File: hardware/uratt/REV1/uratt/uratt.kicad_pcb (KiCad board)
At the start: 4 copper layers, 62 x 71.4 mm, 143 parts, among them J1 USB_B_Micro, J2 Micro_SD_Card, J3 Conn_01x10, J4 Conn_01x04, J5 Conn_01x04, J6 Conn_01x02, J7 Conn_01x02, J8 Conn_01x02, Q1 MMBT3904, Q2 MMBT3904, Q3 2N7002, Q4 DMP31D0U, SW1 SW_Push, SW2 SW_Push, SW3 SW_SPDT, U1 SN65220DBVR, U2 CP2102N-A02-GQFN24, U3 ESP32-WROOM-32E, U4 MCP73832T-2ACI/OT, U5 TPS2115APWR, U6 AP2112K-3.3TRG1, U7 AP2112K-3.3TRG1, U8 TPS61032PWP, U9 MP6513GJ-Z

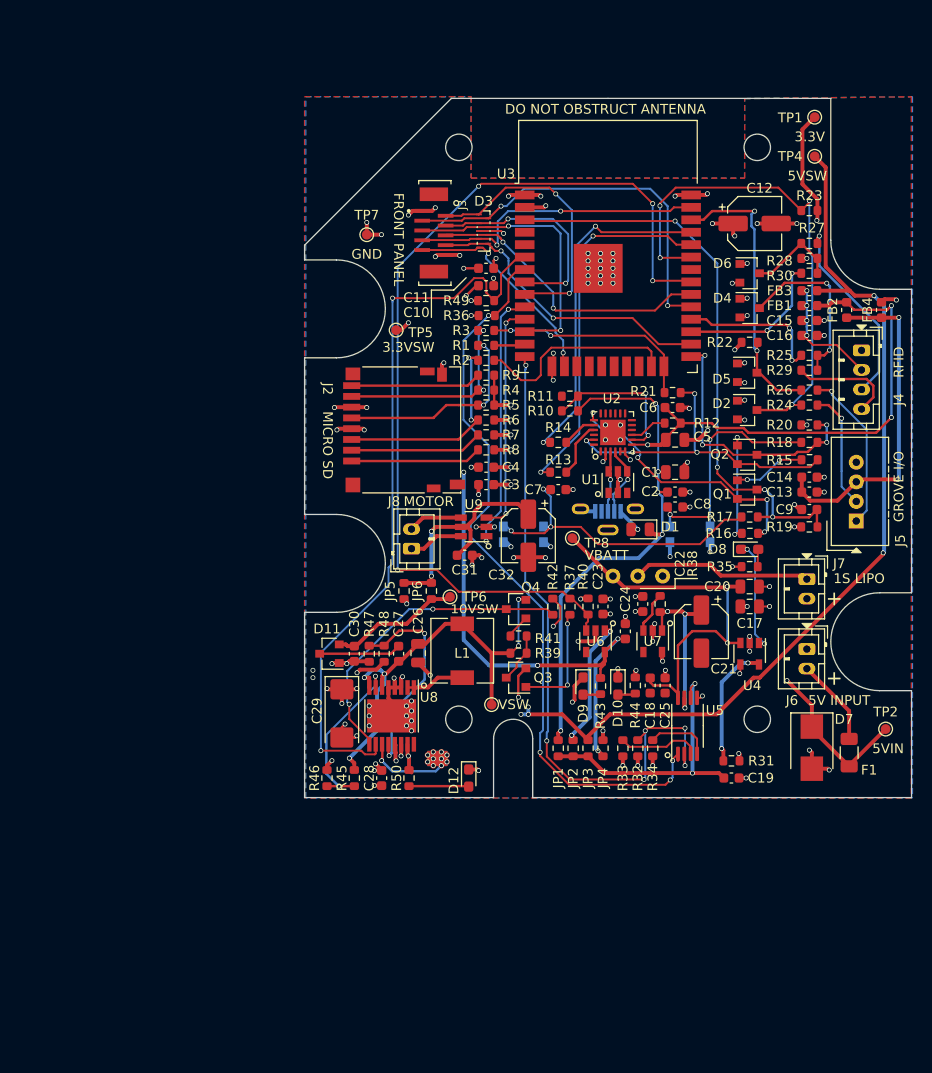
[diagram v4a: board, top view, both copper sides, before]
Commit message: complete relayout of 5V boost switcher, add plated mount holes w/FB GND ties, passes DRC
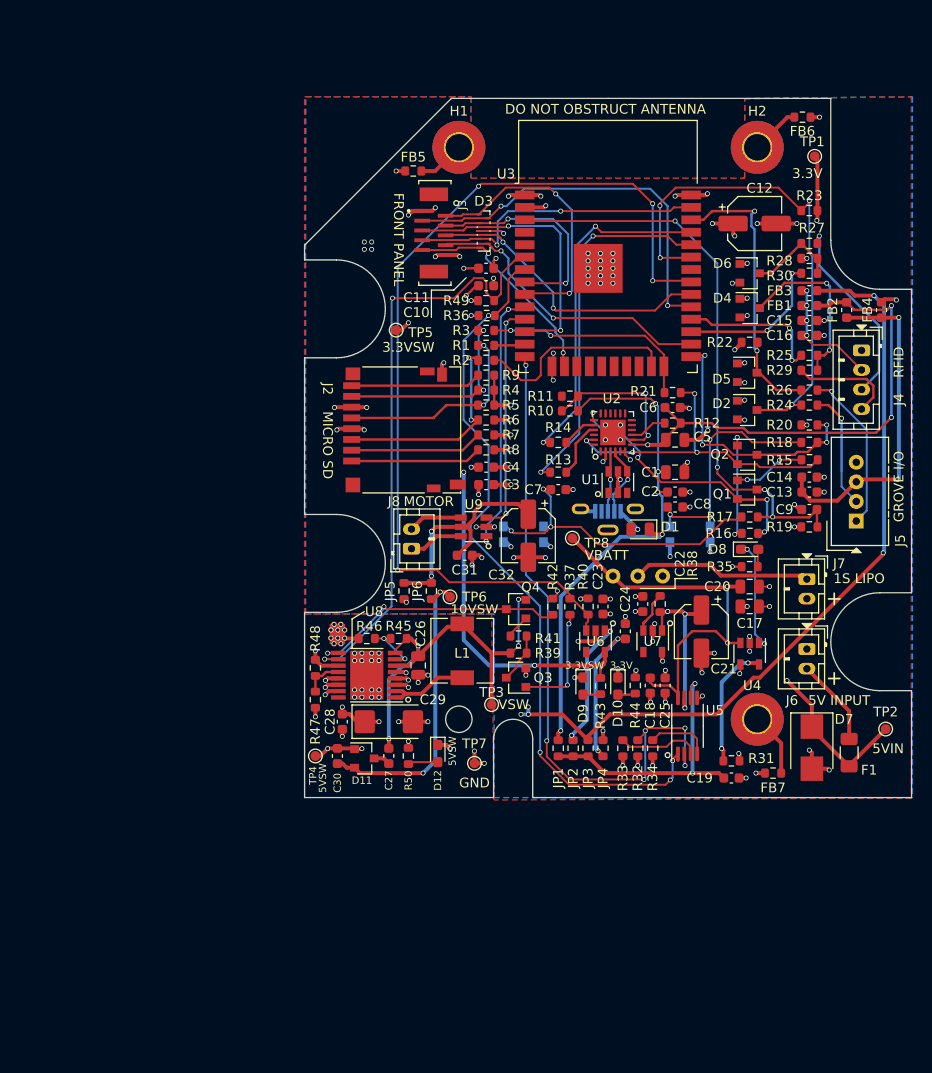
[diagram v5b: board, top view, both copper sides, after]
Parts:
- added FB5: OPTION, Resistor_SMD:R_0603_1608Metric, F.Cu at (36.2, 30.0)
- added FB6: OPTION, Resistor_SMD:R_0603_1608Metric, F.Cu at (76.0, 24.5)
- added FB7: OPTION, Resistor_SMD:R_0603_1608Metric, F.Cu at (73.0, 91.5)
- H1, H2, H4: value MountingHole -> MountingHole_Pad; footprint MountingHole:MountingHole_2.7mm_M2.5 -> MountingHole:MountingHole_2.7mm_M2.5_Pad_TopBottom
- moved TP4 79.7 mm to (26.2, 89.8), turned to 90 degrees
- moved TP7 55.1 mm to (42.5, 90.5)
- moved GT1 17.0 mm to (29.2, 76.9), turned to 270 degrees
- moved R45 15.0 mm to (34.8, 77.8), turned to 0 degrees
- moved R46 14.8 mm to (31.5, 77.8), turned to 0 degrees
- moved D11 11.3 mm to (31.2, 90.0), turned to 0 degrees
- moved C30 10.6 mm to (28.5, 89.8), turned to 90 degrees
- moved C27 10.5 mm to (33.8, 89.8), turned to 90 degrees
- moved R47 7.23 mm to (26.2, 84.0)
- moved R48 7.17 mm to (26.2, 80.8), turned to 270 degrees
- moved C28 7.02 mm to (29.0, 86.2)
- moved U8 4.87 mm to (31.5, 81.5), turned to 90 degrees
- moved C29 4.87 mm to (33.8, 86.2), turned to 0 degrees
- moved D12 4.03 mm to (38.8, 89.5)
- moved TP1 4.00 mm to (77.2, 28.5)
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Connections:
- H1 pad 1: (no net) -> Net-(FB5-Pad2)
- H2 pad 1: (no net) -> Net-(FB6-Pad2)
- H4 pad 1: (no net) -> Net-(FB7-Pad2)
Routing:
- net Net-(R47-Pad1): track 21.6 -> 4.12 mm, vias 2 -> 0
- net +10VSW: track 13.5 -> 30.8 mm, vias 0 -> 2
- net +5VSW: track 112.6 -> 96.2 mm, vias 16 -> 15
- net LOW_BAT: track 75.0 -> 61.0 mm
- net Net-(R45-Pad1): track 17.8 -> 5.63 mm
- net GNDPWR: track 13.3 -> 21.9 mm, vias 22 -> 29
- net Net-(C27-Pad1): track 8.39 -> 1.72 mm
- net Net-(FB7-Pad2): track 0.00 -> 6.51 mm
- net Net-(Q4-Pad3): track 32.3 -> 26.8 mm
- net Net-(FB6-Pad2): track 0.00 -> 5.06 mm
- net +3V3: track 32.7 -> 27.7 mm
- net Net-(FB5-Pad2): track 0.00 -> 4.83 mm
- net GND: track 105.4 -> 102.0 mm, vias 100 -> 108
- net Net-(D12-Pad2): track 6.12 -> 3.08 mm
- net Net-(L1-Pad2): track 6.01 -> 8.84 mm
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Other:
- board text added: "REV1 / 2021-JAN-13"
- board text removed: "REV1 / 20201-XXX-XX"

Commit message: add breakaway rails & fiducials for assembly
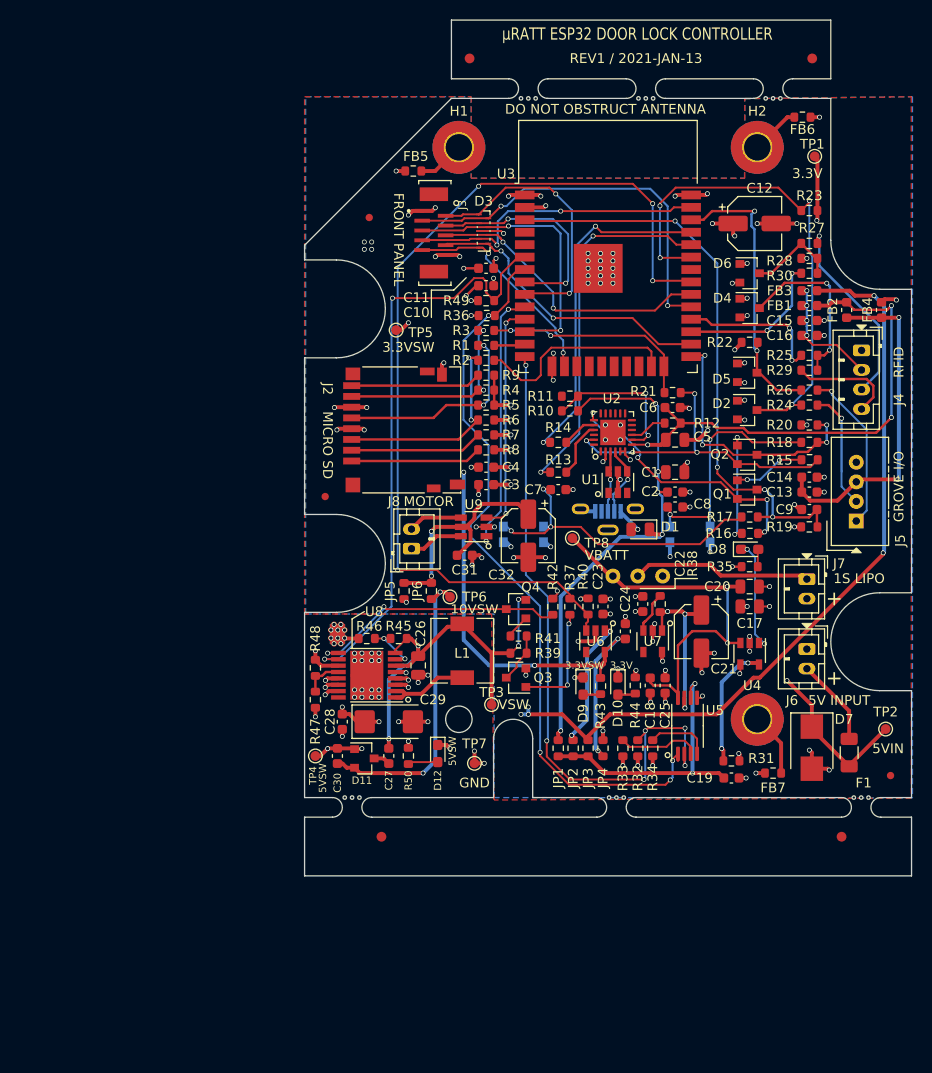
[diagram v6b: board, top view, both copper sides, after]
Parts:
- added BK1: BREAKAWAY, uratt:RATT_BITE, F.Cu at (50.0, 22.6)
- added BK2: BREAKAWAY, uratt:RATT_BITE, F.Cu at (75.0, 22.6)
- added BK3: BREAKAWAY, uratt:RATT_BITE, F.Cu at (62.0, 22.6)
- added BK4: BREAKAWAY, uratt:RATT_BITE, F.Cu at (28.0, 94.0)
- added BK5: BREAKAWAY, uratt:RATT_BITE, F.Cu at (55.0, 94.0)
- added BK6: BREAKAWAY, uratt:RATT_BITE, F.Cu at (80.0, 94.0)
- added FID1: Fiducial, Fiducial:Fiducial_1mm_Mask3mm, F.Cu at (42.0, 18.5)
- added FID2: Fiducial, Fiducial:Fiducial_1mm_Mask3mm, F.Cu at (77.0, 18.5)
- added FID3: Fiducial, Fiducial:Fiducial_1mm_Mask3mm, F.Cu at (33.0, 98.0)
- added FID4: Fiducial, Fiducial:Fiducial_1mm_Mask3mm, F.Cu at (80.0, 98.0)
- added FID5: Fiducial, Fiducial:Fiducial_0.75mm_Mask1.5mm, F.Cu at (31.8, 34.8)
- added FID6: Fiducial, Fiducial:Fiducial_0.75mm_Mask1.5mm, F.Cu at (85.0, 91.8)
- added FID7: Fiducial, Fiducial:Fiducial_0.75mm_Mask1.5mm, F.Cu at (27.2, 63.2)
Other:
- board size 62 x 71.4 mm -> 62 x 87.4 mm

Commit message: uratt REV1 change inductor, cleanups, add 3.3V motor option, silk work, 12 pin FFC
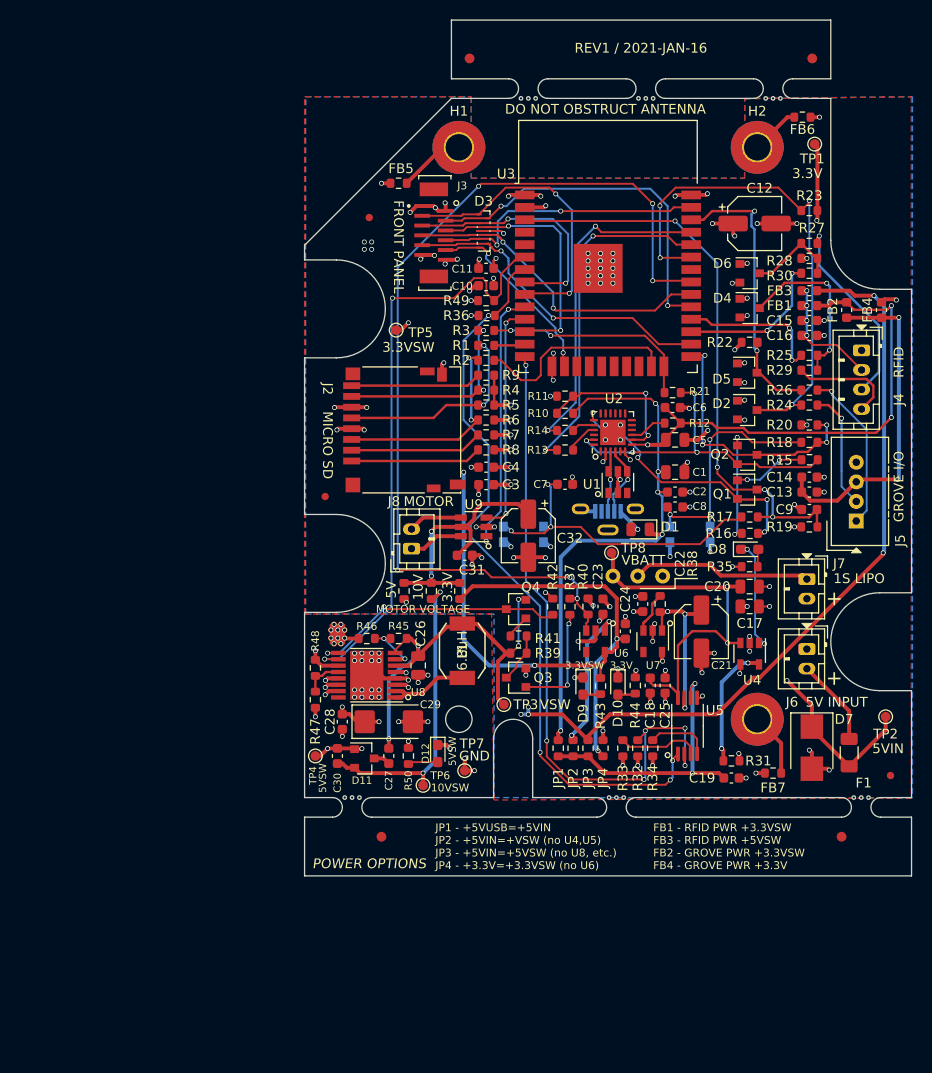
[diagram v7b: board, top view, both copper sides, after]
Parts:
- added JP7: 0 (OPTION), Resistor_SMD:R_0603_1608Metric, F.Cu at (41.0, 72.9)
- J3: footprint uratt:TE_1-1734742-0 -> uratt:TE_1-1734742-2
- L1: footprint Inductor_SMD:L_6.3x6.3_H3 -> uratt:SRR6603-6R8ML
- moved TP6 19.4 mm to (37.2, 92.8)
- moved TP8 4.27 mm to (56.5, 69.0)
- moved R13 2.37 mm to (51.8, 58.5)
- moved FB5 1.95 mm to (34.8, 31.2)
- moved R14 1.40 mm to (51.8, 56.5)
- moved TP1 1.25 mm to (77.2, 27.2)
- moved TP2 1.25 mm to (84.5, 85.8)
- moved TP3 1.25 mm to (45.5, 84.5)
- moved TP7 1.25 mm to (41.5, 91.2)
- moved C7 0.88 mm to (51.8, 62.0)
- moved R10 0.56 mm to (51.8, 54.8)
- moved R11 0.50 mm to (51.8, 53.0)
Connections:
- J3 pad 10: GND -> FP_TOUCH_BTN
- J3 pad 2: LCD_BL -> +3.3VSW
- J3 pad 3: LCD_CS -> LCD_BL
- J3 pad 4: LCD_RESET -> LCD_CS
- J3 pad 5: LCD_DC -> LCD_RESET
- J3 pad 6: LCD_CLK -> LCD_DC
- J3 pad 7: LCD_MOSI -> LCD_CLK
- J3 pad 8: BEEPER -> LCD_MOSI
- J3 pad 9: FP_TOUCH_BTN -> BEEPER
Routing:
- net +3.3VSW: track 125.6 -> 148.2 mm, vias 19 -> 20
- net +VBATT: track 42.1 -> 39.1 mm
- net +5VUSB: track 53.4 -> 56.4 mm
- net Net-(C31-Pad1): track 24.3 -> 27.2 mm
- net Net-(R13-Pad2): track 5.75 -> 3.26 mm
- net LCD_CS: track 39.8 -> 37.4 mm
- net LCD_DC: track 28.3 -> 25.9 mm
- net LCD_RESET: track 22.8 -> 25.2 mm
- net LCD_MOSI: track 30.8 -> 28.4 mm
- net LCD_BL: track 28.3 -> 30.7 mm
- net FP_TOUCH_BTN: track 22.1 -> 19.7 mm
- net BEEPER: track 30.5 -> 32.9 mm
- net LCD_CLK: track 30.0 -> 32.4 mm
- net +VSW: track 75.3 -> 77.7 mm
- net RXD0: track 37.7 -> 35.4 mm
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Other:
- board text added: "10V"
- board text added: "5V"
- board text added: "BOARD NUM."
- board text added: "FB1 - RFID PWR +3.3VSW FB3 - RFID PWR +5VSW FB2 - GROVE PWR +3.3VSW FB4 - GROVE PWR +3.3V"
- board text added: "JP1 - +5VUSB=+5VIN JP2 - +5VIN=+VSW (no U4,U5) JP3 - +5VIN=+5VSW (no U8, etc.) JP4 - +3.3V=+3.3VSW (no U6)"
- board text added: "MOTOR VOLTAGE"
- board text added: "POWER OPTIONS"
- board text added: "REV1 / 2021-JAN-16"
- board text removed: "REV1 / 2021-JAN-13"
